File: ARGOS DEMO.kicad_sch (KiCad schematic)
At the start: 63 parts, among them J1 B2B-XH-A, J2 60312002114503, J3 B4B-XH-A, J4 JTAG 10-PINS, J5 B4B-XH-A, J6 B6B-XH-A, J7 B3B-XH-A, Q1 BSN20, Q2 BSN20, SW1 PTS647, U1 Argos SMD module, U2 LTC4365DDB, U3 TPS63900, U4 TPS63900

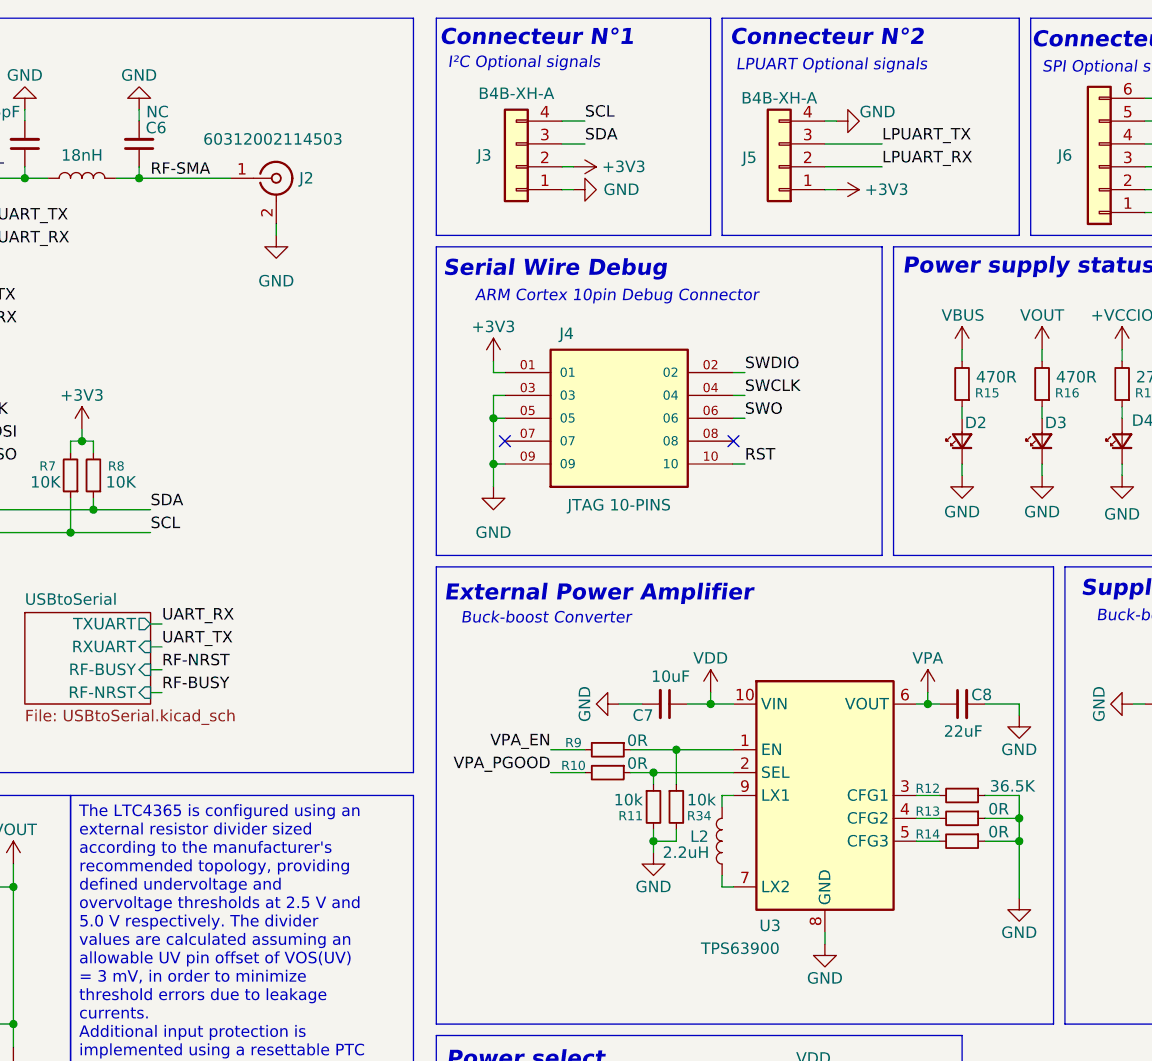
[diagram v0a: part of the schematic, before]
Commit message: Correction USART vers le LPUART
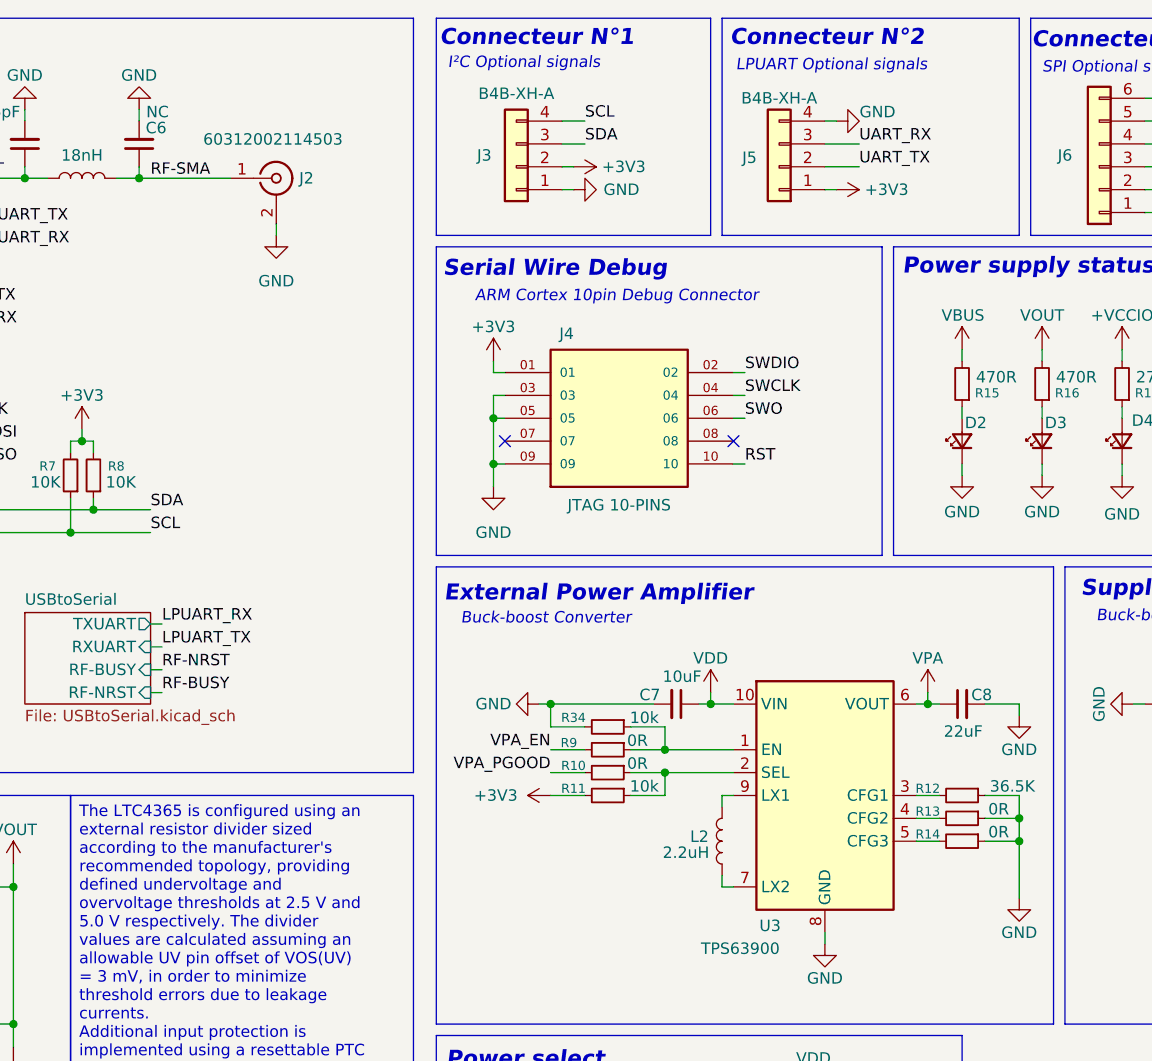
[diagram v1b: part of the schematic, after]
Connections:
- net +3V3: now also R11.2
- net GND: no longer R11.2
- net LPUART_RX: no longer J5.2 (Pin_2)
- net LPUART_TX: no longer J5.3 (Pin_3)
- net UART_RX: now also J5.3 (Pin_3)
- net UART_TX: now also J5.2 (Pin_2)
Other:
- moved on the sheet: C7, R11, R34
